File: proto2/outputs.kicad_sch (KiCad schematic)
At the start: 84 parts, among them Q1 2N7002, Q10 2N7002, Q11 2N7002, Q12 2N7002, Q13 2N7002, Q14 2N7002, Q2 2N7002, Q3 2N7002, Q4 2N7002, Q5 2N7002, Q6 2N7002, Q7 2N7002, Q8 2N7002, Q9 2N7002, U1 AQY282SX, U10 AQY282SX, U11 AQY282SX, U12 AQY282SX, U13 AQY282SX, U14 AQY282SX, U2 AQY282SX, U3 AQY282SX, U4 AQY282SX, U5 AQY282SX, U6 AQY282SX, U7 AQY282SX, U8 AQY282SX, U9 AQY282SX

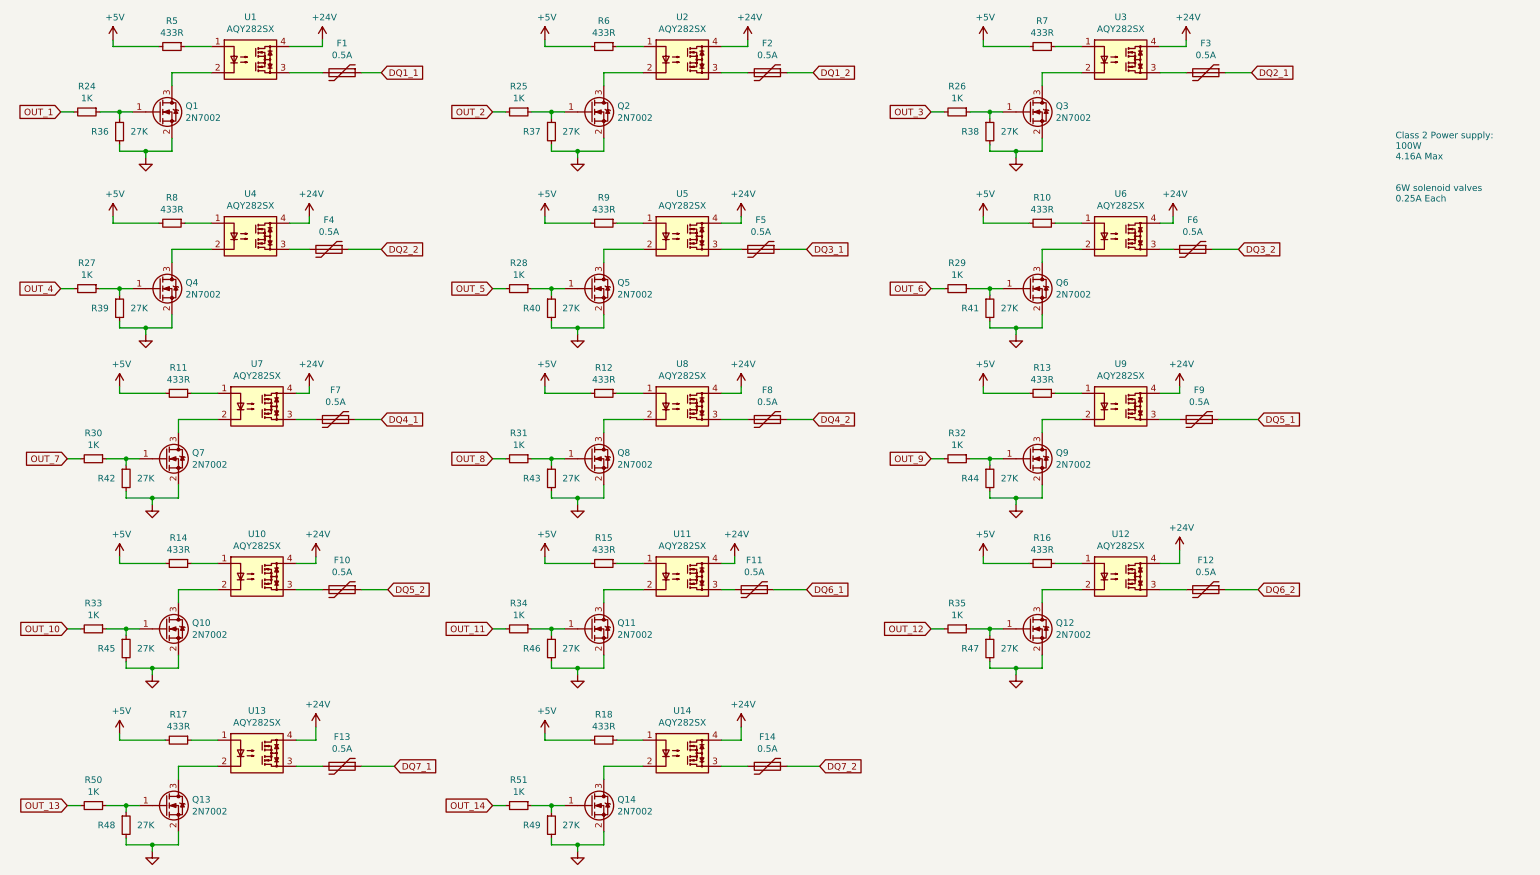
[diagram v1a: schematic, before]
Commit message: Updated F15,D15,U1-14 to parts in stock at JLC. Updated U1-14 footprints to more common size.
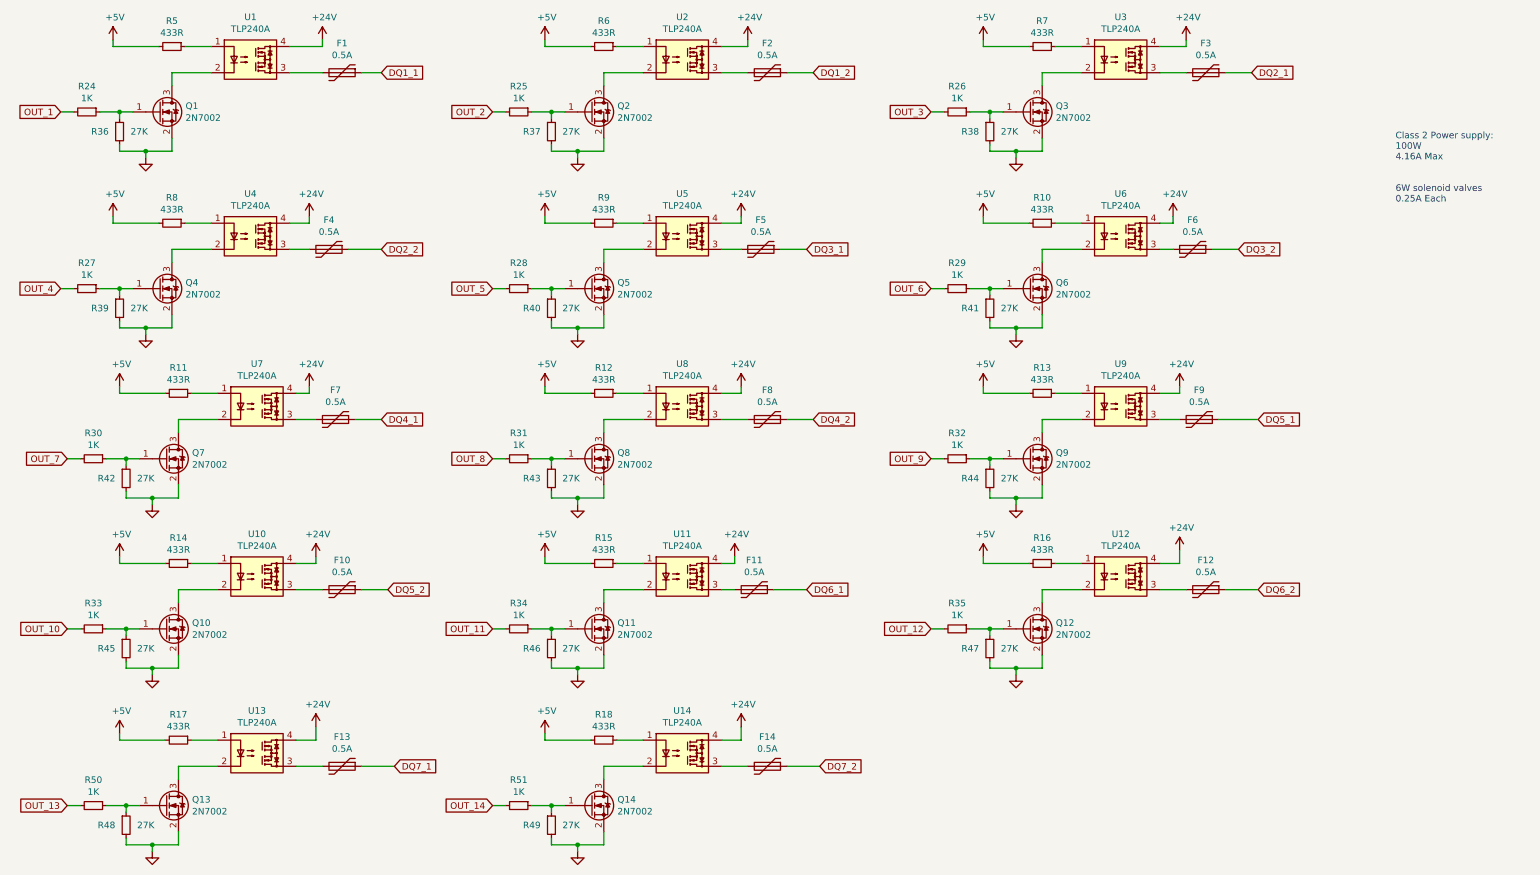
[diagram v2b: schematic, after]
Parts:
- U1, U10, U11, U12, U13, U14, U2, U3, U4, U5, U6, U7, U8, U9: value AQY282SX -> TLP240A; footprint JLCPCB:SO-4_6.0mm_P2.54mm -> JLCPCB:SO-4_8.55mm_P2.54mm; LCSC C250827 -> C146360; Manufacturer (none) -> Toshiba; Part Number (none) -> TLP240A
